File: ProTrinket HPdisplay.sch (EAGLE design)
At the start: 17 parts

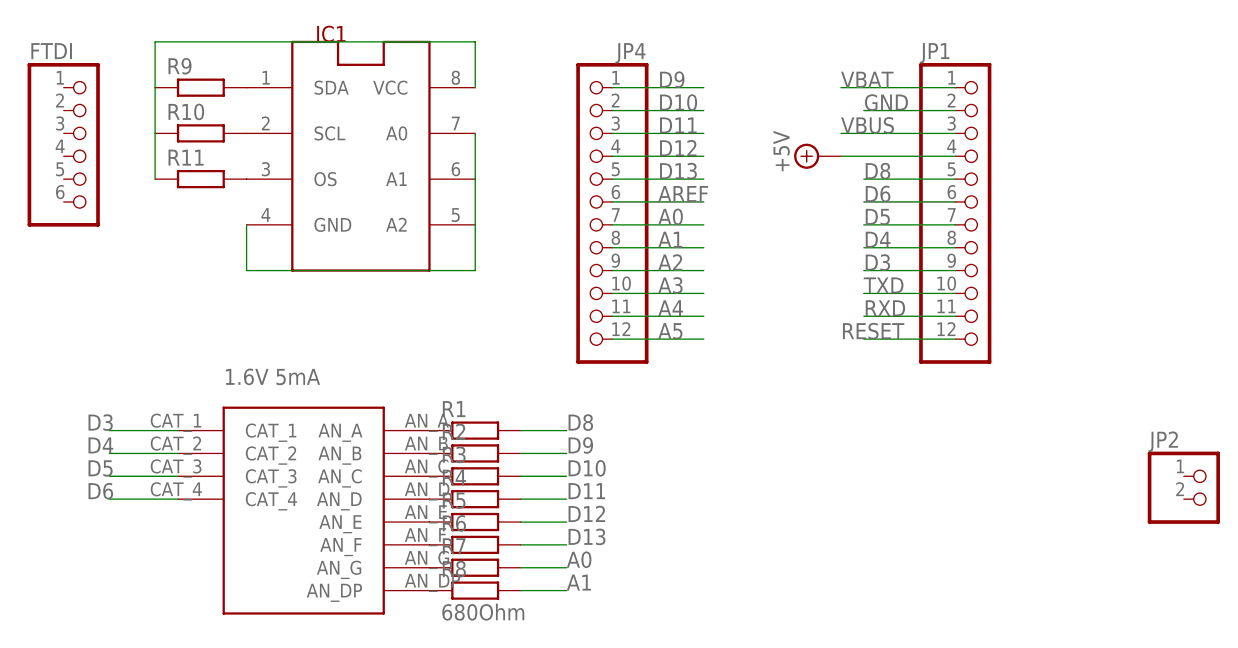
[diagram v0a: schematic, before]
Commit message: fixed IIC connection
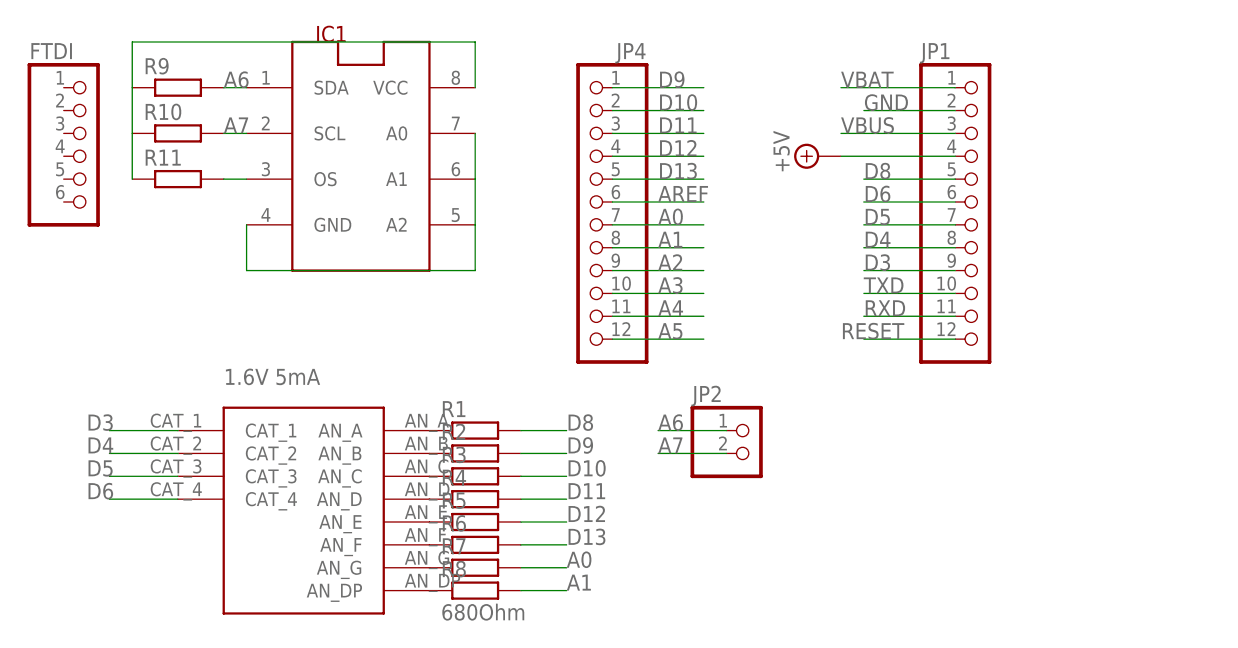
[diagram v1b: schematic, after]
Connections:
- removed net N$10: IC1.SCL, R10.2
- removed net N$13: IC1.SDA, R9.2
- new net A6: IC1.SDA, JP2.1, R9.2
- new net A7: IC1.SCL, JP2.2, R10.2
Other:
- moved on the sheet: JP2, R10, R11, R9
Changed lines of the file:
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@@
 <instance part="FTDI" gate="A" x="76.2" y="185.42"/>
 <instance part="JP1" gate="G$1" x="175.26" y="180.34"/>
-<instance part="JP2" gate="G$1" x="200.66" y="147.32"/>
+<instance part="JP2" gate="G$1" x="149.86" y="152.4"/>
 <instance part="SUPPLY7" gate="+5V" x="157.48" y="185.42" rot="R90"/>
 <instance part="U$1" gate="G$1" x="99.06" y="147.32"/>
@@
 <instance part="R8" gate="G$1" x="119.38" y="137.16"/>
 <instance part="IC1" gate="G$1" x="106.68" y="185.42"/>
-<instance part="R9" gate="G$1" x="88.9" y="193.04"/>
-<instance part="R10" gate="G$1" x="88.9" y="187.96"/>
-<instance part="R11" gate="G$1" x="88.9" y="182.88"/>
+<instance part="R9" gate="G$1" x="86.36" y="193.04"/>
+<instance part="R10" gate="G$1" x="86.36" y="187.96"/>
+<instance part="R11" gate="G$1" x="86.36" y="182.88"/>
 </instances>
 <busses>
@@
 <pinref part="R11" gate="G$1" pin="1"/>
 <pinref part="R10" gate="G$1" pin="1"/>
-<wire x1="83.82" y1="182.88" x2="83.82" y2="187.96" width="0.1524" layer="91"/>
+<wire x1="81.28" y1="182.88" x2="81.28" y2="187.96" width="0.1524" layer="91"/>
 <pinref part="R9" gate="G$1" pin="1"/>
-<wire x1="83.82" y1="187.96" x2="83.82" y2="193.04" width="0.1524" layer="91"/>
-<wire x1="83.82" y1="193.04" x2="83.82" y2="198.12" width="0.1524" layer="91"/>
+<wire x1="81.28" y1="187.96" x2="81.28" y2="193.04" width="0.1524" layer="91"/>
+<wire x1="81.28" y1="193.04" x2="81.28" y2="198.12" width="0.1524" layer="91"/>
 <pinref part="IC1" gate="G$1" pin="VCC"/>
-<wire x1="83.82" y1="198.12" x2="119.38" y2="198.12" width="0.1524" layer="91"/>
+<wire x1="81.28" y1="198.12" x2="119.38" y2="198.12" width="0.1524" layer="91"/>
 <wire x1="119.38" y1="198.12" x2="119.38" y2="193.04" width="0.1524" layer="91"/>
 </segment>
@@
 </segment>
 </net>
-<net name="N$10" class="0">
+<net name="A7" class="0">
 <segment>
 <pinref part="IC1" gate="G$1" pin="SCL"/>
 <pinref part="R10" gate="G$1" pin="2"/>
+<wire x1="91.44" y1="187.96" x2="93.98" y2="187.96" width="0.1524" layer="91"/>
+<label x="91.44" y="187.96" size="1.778" layer="95"/>
+</segment>
+<segment>
+<pinref part="JP2" gate="G$1" pin="2"/>
+<wire x1="147.32" y1="152.4" x2="139.7" y2="152.4" width="0.1524" layer="91"/>
+<label x="139.7" y="152.4" size="1.778" layer="95"/>
 </segment>
 </net>
@@
 <pinref part="IC1" gate="G$1" pin="OS"/>
 <pinref part="R11" gate="G$1" pin="2"/>
-</segment>
-</net>
-<net name="N$13" class="0">
+<wire x1="91.44" y1="182.88" x2="93.98" y2="182.88" width="0.1524" layer="91"/>
+</segment>
+</net>
+<net name="A6" class="0">
+<segment>
+<pinref part="JP2" gate="G$1" pin="1"/>
+<wire x1="147.32" y1="154.94" x2="139.7" y2="154.94" width="0.1524" layer="91"/>
+<label x="139.7" y="154.94" size="1.778" layer="95"/>
+</segment>
 <segment>
 <pinref part="IC1" gate="G$1" pin="SDA"/>
 <pinref part="R9" gate="G$1" pin="2"/>
-</segment>
-</net>
+<wire x1="91.44" y1="193.04" x2="93.98" y2="193.04" width="0.1524" layer="91"/>
+<label x="91.44" y="193.04" size="1.778" layer="95"/>
+</segment>
+</net>

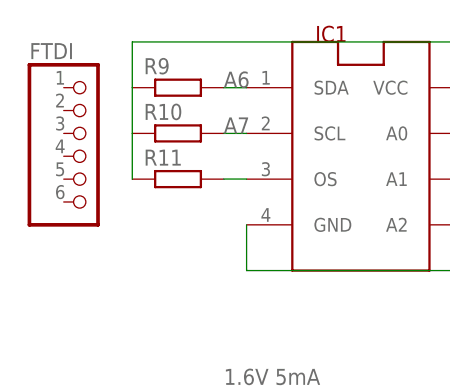
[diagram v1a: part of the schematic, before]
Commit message: removed vias
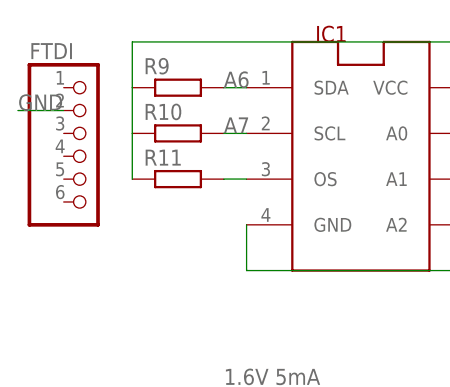
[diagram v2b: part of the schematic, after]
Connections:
- net GND: now also FTDI.2
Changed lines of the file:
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@@
 <wire x1="119.38" y1="172.72" x2="119.38" y2="177.8" width="0.1524" layer="91"/>
+</segment>
+<segment>
+<pinref part="FTDI" gate="A" pin="2"/>
+<wire x1="73.66" y1="190.5" x2="68.58" y2="190.5" width="0.1524" layer="91"/>
+<label x="68.58" y="190.5" size="1.778" layer="95"/>
 </segment>
 </net>

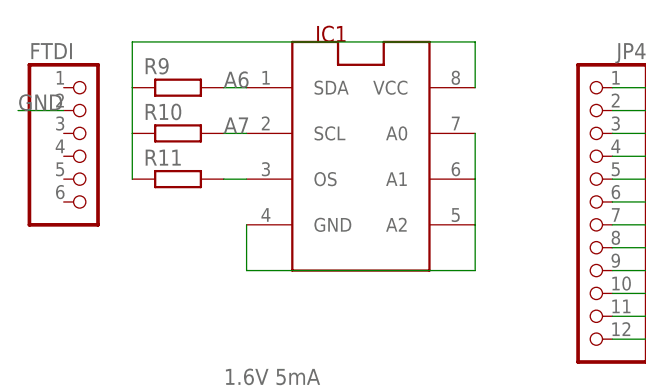
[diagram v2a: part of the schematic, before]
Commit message: mixed up IIC lines
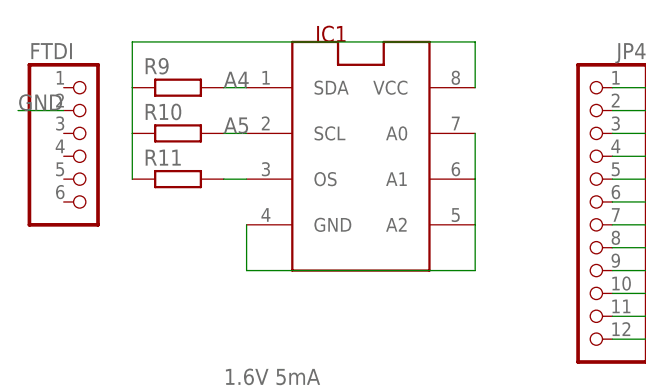
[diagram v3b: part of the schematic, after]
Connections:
- net A4: now also IC1.SDA, R9.2
- net A5: now also IC1.SCL, R10.2
- net A6: no longer IC1.SDA, R9.2
- net A7: no longer IC1.SCL, R10.2
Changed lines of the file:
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@@
 <label x="139.7" y="167.64" size="1.778" layer="95"/>
+</segment>
+<segment>
+<pinref part="IC1" gate="G$1" pin="SDA"/>
+<pinref part="R9" gate="G$1" pin="2"/>
+<wire x1="91.44" y1="193.04" x2="93.98" y2="193.04" width="0.1524" layer="91"/>
+<label x="91.44" y="193.04" size="1.778" layer="95"/>
 </segment>
 </net>
@@
 <wire x1="134.62" y1="165.1" x2="144.78" y2="165.1" width="0.1524" layer="91"/>
 <label x="139.7" y="165.1" size="1.778" layer="95"/>
+</segment>
+<segment>
+<pinref part="IC1" gate="G$1" pin="SCL"/>
+<pinref part="R10" gate="G$1" pin="2"/>
+<wire x1="91.44" y1="187.96" x2="93.98" y2="187.96" width="0.1524" layer="91"/>
+<label x="91.44" y="187.96" size="1.778" layer="95"/>
 </segment>
 </net>
@@
 <net name="A7" class="0">
 <segment>
-<pinref part="IC1" gate="G$1" pin="SCL"/>
-<pinref part="R10" gate="G$1" pin="2"/>
-<wire x1="91.44" y1="187.96" x2="93.98" y2="187.96" width="0.1524" layer="91"/>
-<label x="91.44" y="187.96" size="1.778" layer="95"/>
-</segment>
-<segment>
 <pinref part="JP2" gate="G$1" pin="2"/>
 <wire x1="147.32" y1="152.4" x2="139.7" y2="152.4" width="0.1524" layer="91"/>
@@
 <label x="139.7" y="154.94" size="1.778" layer="95"/>
 </segment>
-<segment>
-<pinref part="IC1" gate="G$1" pin="SDA"/>
-<pinref part="R9" gate="G$1" pin="2"/>
-<wire x1="91.44" y1="193.04" x2="93.98" y2="193.04" width="0.1524" layer="91"/>
-<label x="91.44" y="193.04" size="1.778" layer="95"/>
-</segment>
-</net>
+</net>
